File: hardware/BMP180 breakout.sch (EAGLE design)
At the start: 15 parts, among them U1 BMP180

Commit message: Review for reds
Minor updates to PCB, updated library and example code, added datasheet
and readme
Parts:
- removed LOGO3: LOGO-SFESK, SparkFun-Aesthetics:LOGO-SFESK
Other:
- note added: "1.0"
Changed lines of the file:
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@@
 <part name="LOGO1" library="SparkFun-Aesthetics" deviceset="LOGO-SFE" device="NW2"/>
 <part name="LOGO2" library="SparkFun-Aesthetics" deviceset="OSHW-LOGO" device="S"/>
-<part name="LOGO3" library="SparkFun-Aesthetics" deviceset="LOGO-SFE" device="SK"/>
 <part name="STANDOFF1" library="SparkFun-Electromechanical" deviceset="STAND-OFF" device=""/>
 <part name="STANDOFF2" library="SparkFun-Electromechanical" deviceset="STAND-OFF" device=""/>
@@
 <rectangle x1="94.615" y1="118.745" x2="98.425" y2="120.015" layer="94"/>
 <rectangle x1="159.385" y1="116.205" x2="160.655" y2="117.475" layer="94"/>
-<text x="172.72" y="7.62" size="2.54" layer="94">M Grusin</text>
+<text x="175.26" y="7.62" size="2.54" layer="94">M Grusin</text>
 <text x="104.14" y="119.38" size="1.778" layer="97">SHORT BOTH SIDES OF SJ1</text>
 <text x="104.14" y="116.84" size="1.778" layer="97">TO ENABLE PULL-UP RESISTORS</text>
@@
 <text x="167.64" y="119.38" size="1.778" layer="97">SHORT SJ2 TO CONNECT VDD</text>
 <text x="167.64" y="116.84" size="1.778" layer="97">AND VDDIO TOGETHER</text>
+<text x="238.76" y="7.62" size="2.54" layer="94">1.0</text>
 </plain>
 <instances>
@@
 <instance part="GND4" gate="1" x="165.1" y="78.74"/>
 <instance part="SUPPLY4" gate="1" x="96.52" y="127"/>
-<instance part="LOGO1" gate="G$1" x="137.16" y="7.62"/>
-<instance part="LOGO2" gate="G$1" x="132.08" y="25.4"/>
-<instance part="LOGO3" gate="G$1" x="124.46" y="7.62"/>
-<instance part="STANDOFF1" gate="G$1" x="114.3" y="7.62"/>
-<instance part="STANDOFF2" gate="G$1" x="114.3" y="12.7"/>
+<instance part="LOGO1" gate="G$1" x="241.3" y="17.78"/>
+<instance part="LOGO2" gate="G$1" x="132.08" y="12.7"/>
+<instance part="STANDOFF1" gate="G$1" x="236.22" y="20.32"/>
+<instance part="STANDOFF2" gate="G$1" x="236.22" y="17.78"/>
 </instances>
 <busses>

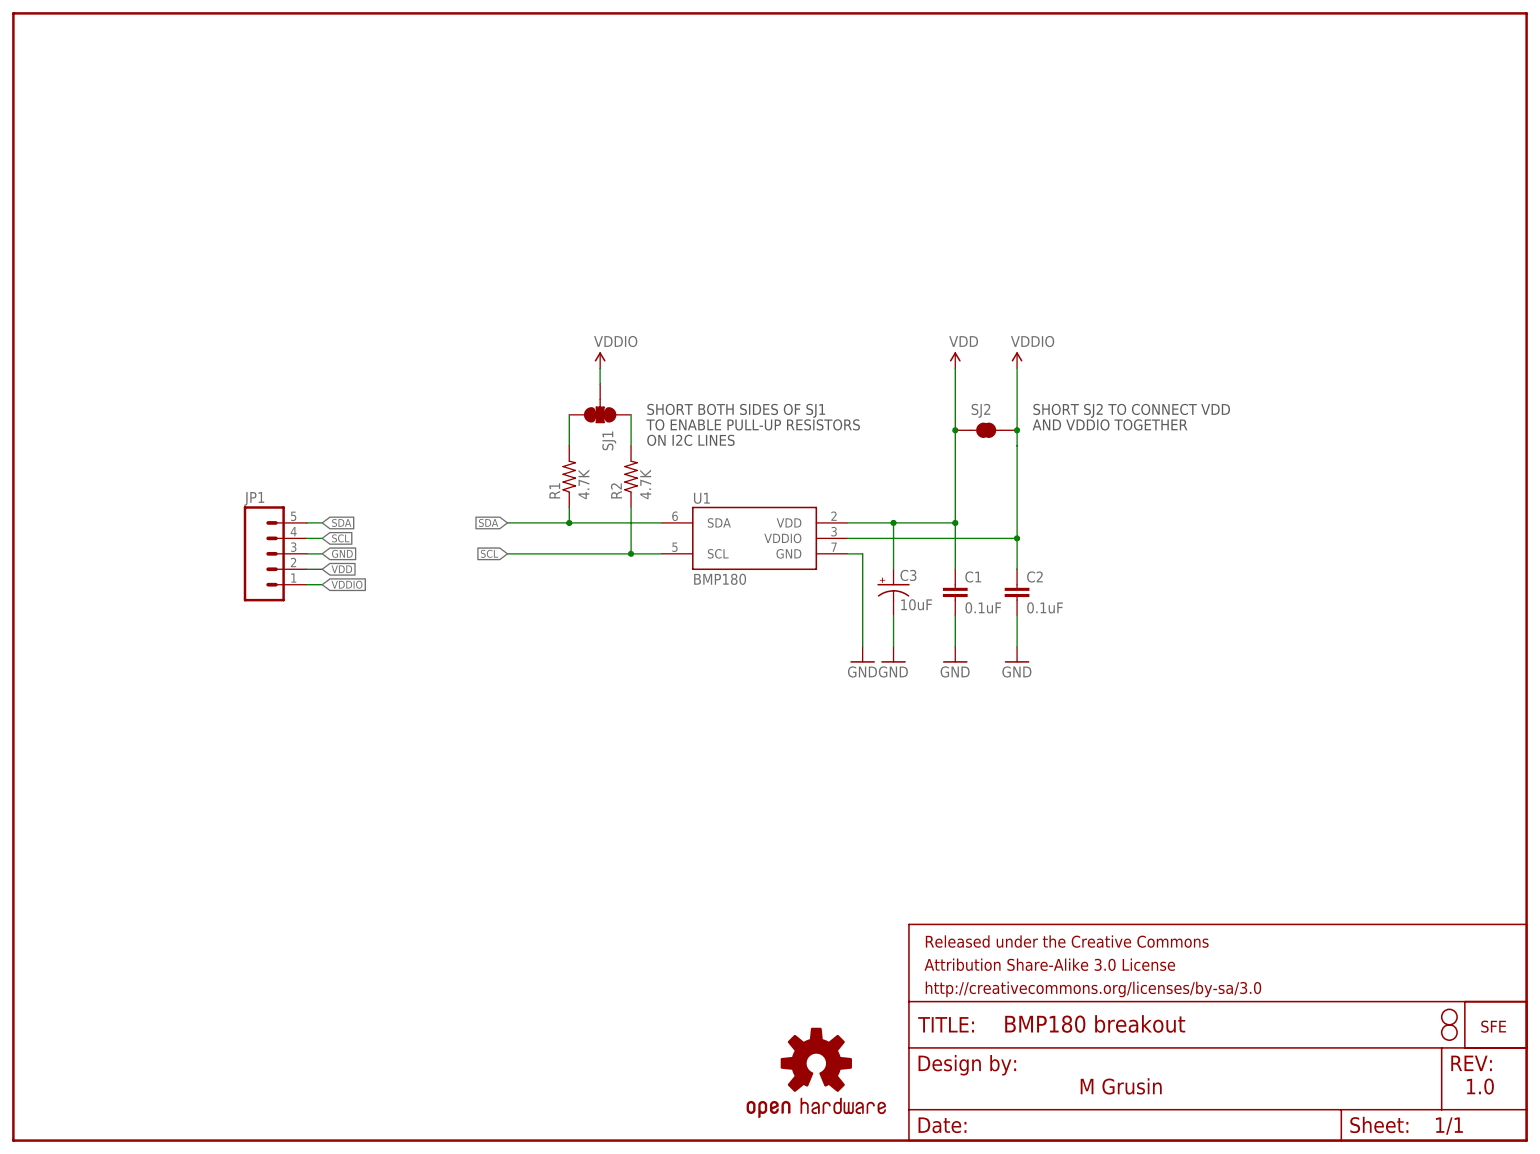
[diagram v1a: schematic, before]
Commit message: Minor changes for reds (V10)
Added silk to solder jumpers
Added BMP180 part to SparkFun Eagle Libraries
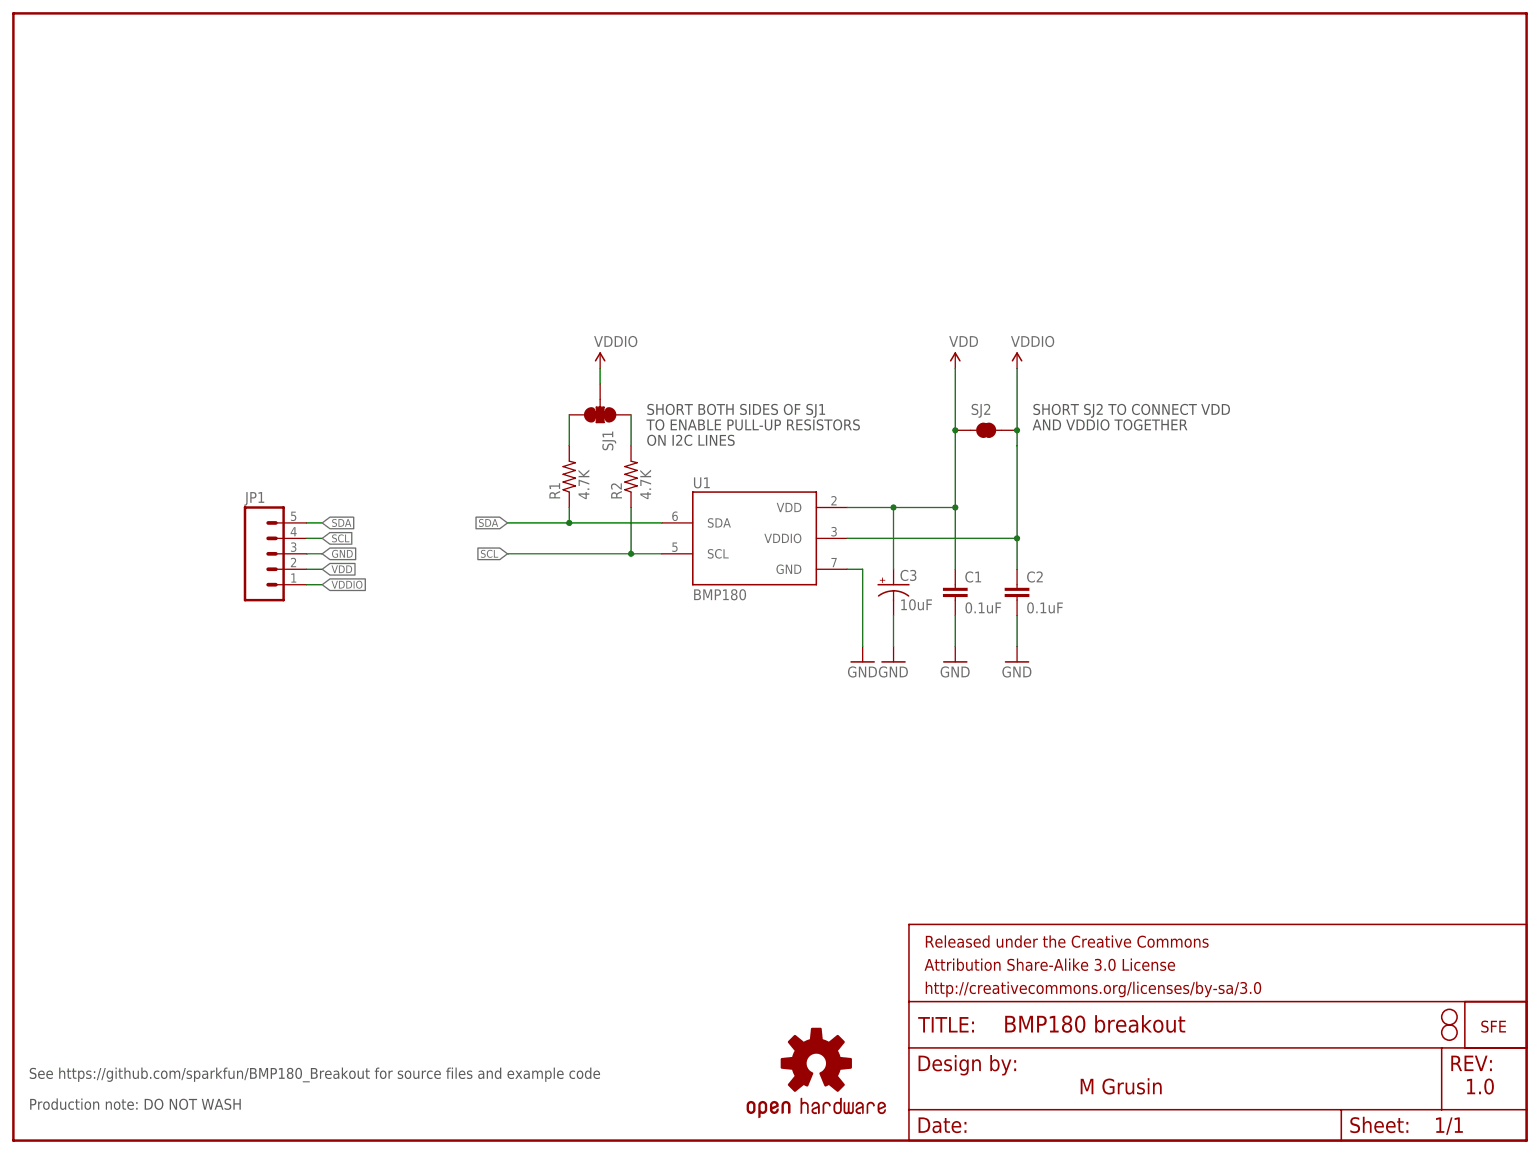
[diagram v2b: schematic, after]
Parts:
- U1: device mike-temp:BMP180 -> SparkFun-Sensors:BMP180
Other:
- note added: "Production note: DO NOT WASH"
- note added: "See https://github.com/sparkfun/BMP180_Breakout for source files and example code"
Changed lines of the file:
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@@
 <layer number="106" name="bPlate" color="7" fill="1" visible="no" active="yes"/>
 <layer number="107" name="Crop" color="7" fill="1" visible="no" active="yes"/>
+<layer number="108" name="tplace-old" color="10" fill="1" visible="yes" active="yes"/>
+<layer number="109" name="ref-old" color="11" fill="1" visible="yes" active="yes"/>
 <layer number="116" name="Patch_BOT" color="9" fill="4" visible="no" active="yes"/>
 <layer number="121" name="_tsilk" color="7" fill="1" visible="no" active="yes"/>
@@
 <parts>
 <part name="FRAME1" library="SparkFun-Aesthetics" deviceset="FRAME-LETTER" device=""/>
-<part name="U1" library="mike-temp" deviceset="BMP180" device=""/>
+<part name="U1" library="SparkFun-Sensors" deviceset="BMP180" device=""/>
 <part name="SJ1" library="mike-temp" deviceset="SOLDERJUMPER_2WAY" device="PASTE1&amp;2&amp;3"/>
 <part name="R1" library="SparkFun-Passives" deviceset="RESISTOR" device="0603-RES" value="4.7K"/>
@@
 <text x="167.64" y="116.84" size="1.778" layer="97">AND VDDIO TOGETHER</text>
 <text x="238.76" y="7.62" size="2.54" layer="94">1.0</text>
+<text x="2.54" y="5.08" size="1.778" layer="97">Production note: DO NOT WASH</text>
+<text x="2.54" y="10.16" size="1.778" layer="97">See https://github.com/sparkfun/BMP180_Breakout for source files and example code</text>
 </plain>
 <instances>
@@
 <pinref part="SUPPLY2" gate="1" pin="VCC"/>
 <pinref part="U1" gate="G$1" pin="VDD"/>
-<wire x1="137.16" y1="101.6" x2="144.78" y2="101.6" width="0.1524" layer="91"/>
-<wire x1="144.78" y1="101.6" x2="154.94" y2="101.6" width="0.1524" layer="91"/>
-<wire x1="154.94" y1="101.6" x2="154.94" y2="93.98" width="0.1524" layer="91"/>
-<junction x="144.78" y="101.6"/>
-<wire x1="144.78" y1="101.6" x2="144.78" y2="93.98" width="0.1524" layer="91"/>
+<wire x1="137.16" y1="104.14" x2="144.78" y2="104.14" width="0.1524" layer="91"/>
+<wire x1="144.78" y1="104.14" x2="154.94" y2="104.14" width="0.1524" layer="91"/>
+<wire x1="154.94" y1="104.14" x2="154.94" y2="93.98" width="0.1524" layer="91"/>
+<junction x="144.78" y="104.14"/>
+<wire x1="144.78" y1="104.14" x2="144.78" y2="93.98" width="0.1524" layer="91"/>
 <pinref part="C3" gate="G$1" pin="+"/>
 <pinref part="C1" gate="G$1" pin="1"/>
-<wire x1="154.94" y1="116.84" x2="154.94" y2="101.6" width="0.1524" layer="91"/>
-<junction x="154.94" y="101.6"/>
+<wire x1="154.94" y1="116.84" x2="154.94" y2="104.14" width="0.1524" layer="91"/>
+<junction x="154.94" y="104.14"/>
 </segment>
 <segment>
@@
 <segment>
 <pinref part="U1" gate="G$1" pin="GND"/>
-<wire x1="137.16" y1="96.52" x2="139.7" y2="96.52" width="0.1524" layer="91"/>
-<wire x1="139.7" y1="96.52" x2="139.7" y2="81.28" width="0.1524" layer="91"/>
+<wire x1="137.16" y1="93.98" x2="139.7" y2="93.98" width="0.1524" layer="91"/>
+<wire x1="139.7" y1="93.98" x2="139.7" y2="81.28" width="0.1524" layer="91"/>
 <pinref part="GND1" gate="1" pin="GND"/>
 </segment>

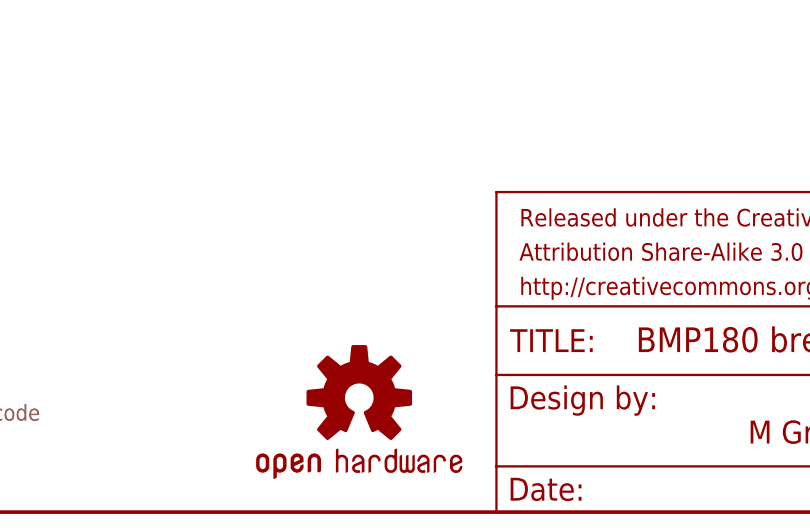
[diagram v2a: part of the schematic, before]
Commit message: Added microfiducials
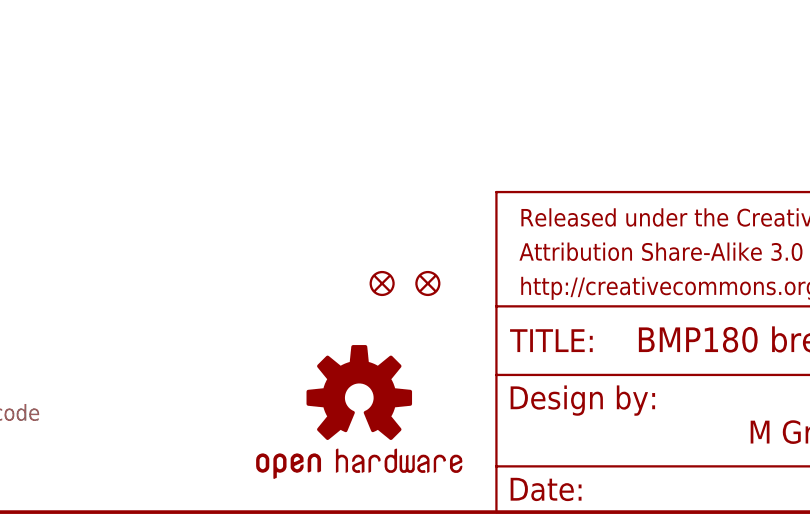
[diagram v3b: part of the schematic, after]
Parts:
- added FID1, FID2: FIDUCIALUFIDUCIAL, SparkFun-Aesthetics:FIDUCIALUFIDUCIAL
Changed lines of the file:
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@@
 <part name="STANDOFF1" library="SparkFun-Electromechanical" deviceset="STAND-OFF" device=""/>
 <part name="STANDOFF2" library="SparkFun-Electromechanical" deviceset="STAND-OFF" device=""/>
+<part name="FID1" library="SparkFun-Aesthetics" deviceset="FIDUCIAL" device="UFIDUCIAL"/>
+<part name="FID2" library="SparkFun-Aesthetics" deviceset="FIDUCIAL" device="UFIDUCIAL"/>
 </parts>
 <sheets>
@@
 <instance part="STANDOFF1" gate="G$1" x="236.22" y="20.32"/>
 <instance part="STANDOFF2" gate="G$1" x="236.22" y="17.78"/>
+<instance part="FID1" gate="G$1" x="139.7" y="25.4"/>
+<instance part="FID2" gate="G$1" x="134.62" y="25.4"/>
 </instances>
 <busses>
